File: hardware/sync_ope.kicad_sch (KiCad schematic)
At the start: 56 parts

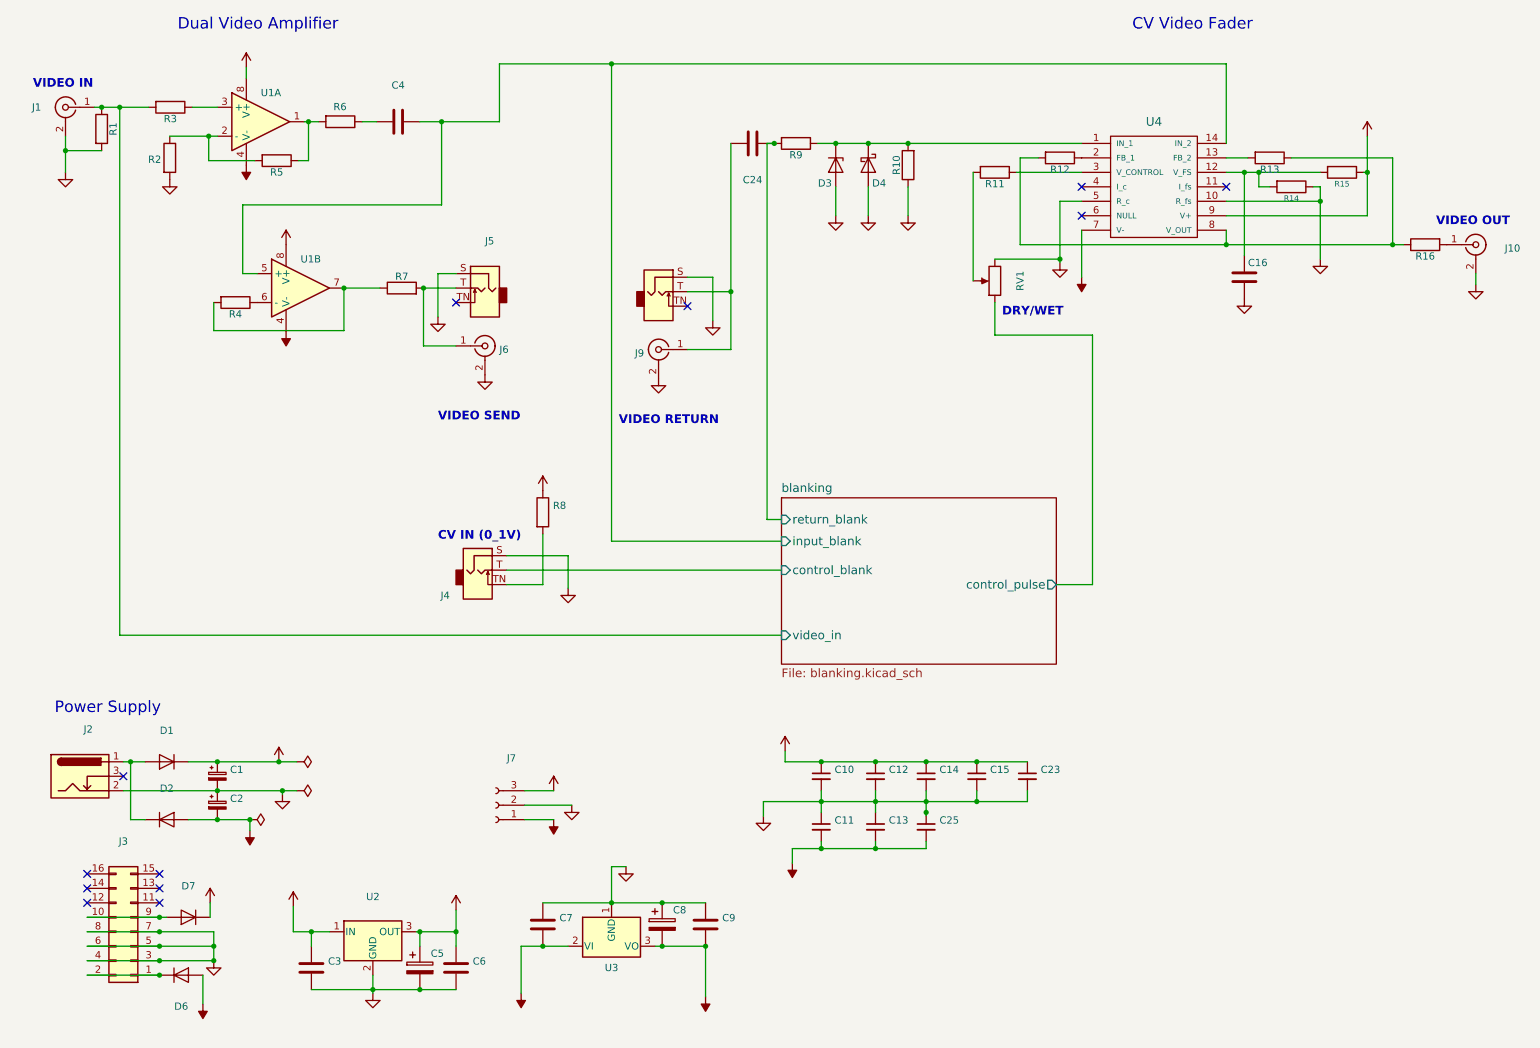
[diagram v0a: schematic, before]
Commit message: update blanking values
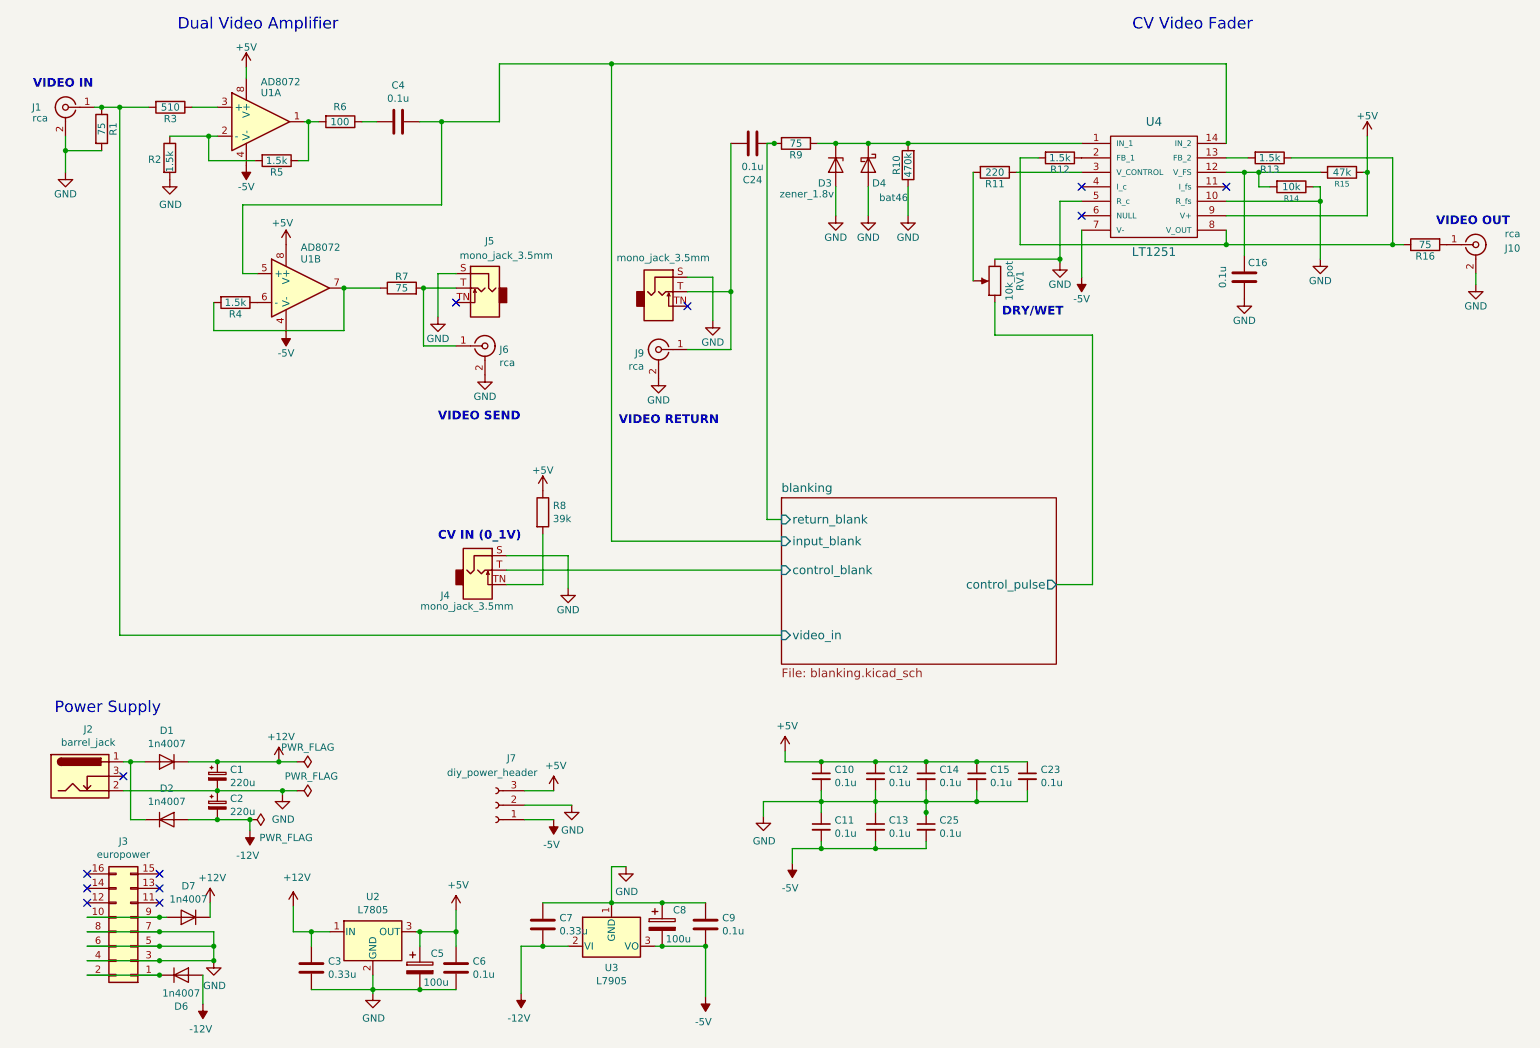
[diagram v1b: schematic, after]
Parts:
- C1, C2: value (none) -> 220u; footprint (none) -> Capacitor_THT:CP_Radial_D7.5mm_P2.50mm
- C10, C11, C12, C13, C14, C15, C16, C23, C24, C25, C4, C6, C9: value (none) -> 0.1u; footprint (none) -> Capacitor_THT:C_Disc_D4.3mm_W1.9mm_P5.00mm
- C3, C7: value (none) -> 0.33u; footprint (none) -> Capacitor_THT:C_Disc_D4.3mm_W1.9mm_P5.00mm
- C5, C8: value (none) -> 100u; footprint (none) -> Capacitor_THT:CP_Radial_D7.5mm_P2.50mm
- D1, D2, D6, D7: value (none) -> 1n4007; footprint (none) -> Diode_THT:D_DO-35_SOD27_P10.16mm_Horizontal
- D3: value (none) -> zener_1.8v; footprint (none) -> Diode_THT:D_DO-35_SOD27_P7.62mm_Horizontal
- D4: value (none) -> bat46; footprint (none) -> Diode_THT:D_DO-35_SOD27_P7.62mm_Horizontal
- J1, J10, J6, J9: value (none) -> rca; footprint (none) -> lib_fp:tht_vertical_rca
- J2: value (none) -> barrel_jack; footprint (none) -> Connector_BarrelJack:BarrelJack_Horizontal
- J3: value (none) -> europower; footprint (none) -> Connector_PinHeader_2.54mm:PinHeader_2x08_P2.54mm_Vertical
- J4, J5: value (none) -> mono_jack_3.5mm; footprint (none) -> lib_fp:Jack_3.5mm_QingPu_WQP-PJ398SM_Vertical_CircularHoles
- J7: value (none) -> diy_power_header; footprint (none) -> Connector_PinHeader_2.54mm:PinHeader_1x03_P2.54mm_Vertical
- J8: value (none) -> mono_jack_3.5mm; footprint (none) -> Connector_Audio:Jack_3.5mm_QingPu_WQP-PJ398SM_Vertical_CircularHoles
- R1, R16, R7, R9: value (none) -> 75; footprint (none) -> Resistor_THT:R_Axial_DIN0204_L3.6mm_D1.6mm_P7.62mm_Horizontal
- R10: value (none) -> 470k; footprint (none) -> Resistor_THT:R_Axial_DIN0204_L3.6mm_D1.6mm_P7.62mm_Horizontal
- R11: value (none) -> 220; footprint (none) -> Resistor_THT:R_Axial_DIN0204_L3.6mm_D1.6mm_P7.62mm_Horizontal
- R12, R13, R2, R4, R5: value (none) -> 1.5k; footprint (none) -> Resistor_THT:R_Axial_DIN0204_L3.6mm_D1.6mm_P7.62mm_Horizontal
- R14: value (none) -> 10k; footprint (none) -> Resistor_THT:R_Axial_DIN0204_L3.6mm_D1.6mm_P7.62mm_Horizontal
- R15: value (none) -> 47k; footprint (none) -> Resistor_THT:R_Axial_DIN0204_L3.6mm_D1.6mm_P7.62mm_Horizontal
- R3: value (none) -> 510; footprint (none) -> Resistor_THT:R_Axial_DIN0204_L3.6mm_D1.6mm_P7.62mm_Horizontal
- R6: value (none) -> 100; footprint (none) -> Resistor_THT:R_Axial_DIN0204_L3.6mm_D1.6mm_P7.62mm_Horizontal
- R8: value (none) -> 39k; footprint (none) -> Resistor_THT:R_Axial_DIN0204_L3.6mm_D1.6mm_P7.62mm_Horizontal
- RV1: value (none) -> 10k_pot; footprint (none) -> lib_fp:Potentiometer_Vertical_Large
- U1: value (none) -> AD8072; footprint (none) -> lib_fp:DIP-SOIC-8
- U2: value (none) -> L7805; footprint (none) -> Package_TO_SOT_THT:TO-220-3_Vertical
- U3: value (none) -> L7905; footprint (none) -> Package_TO_SOT_THT:TO-220-3_Vertical
- U4: value (none) -> LT1251; footprint (none) -> lib_fp:DIP+SOIC_14

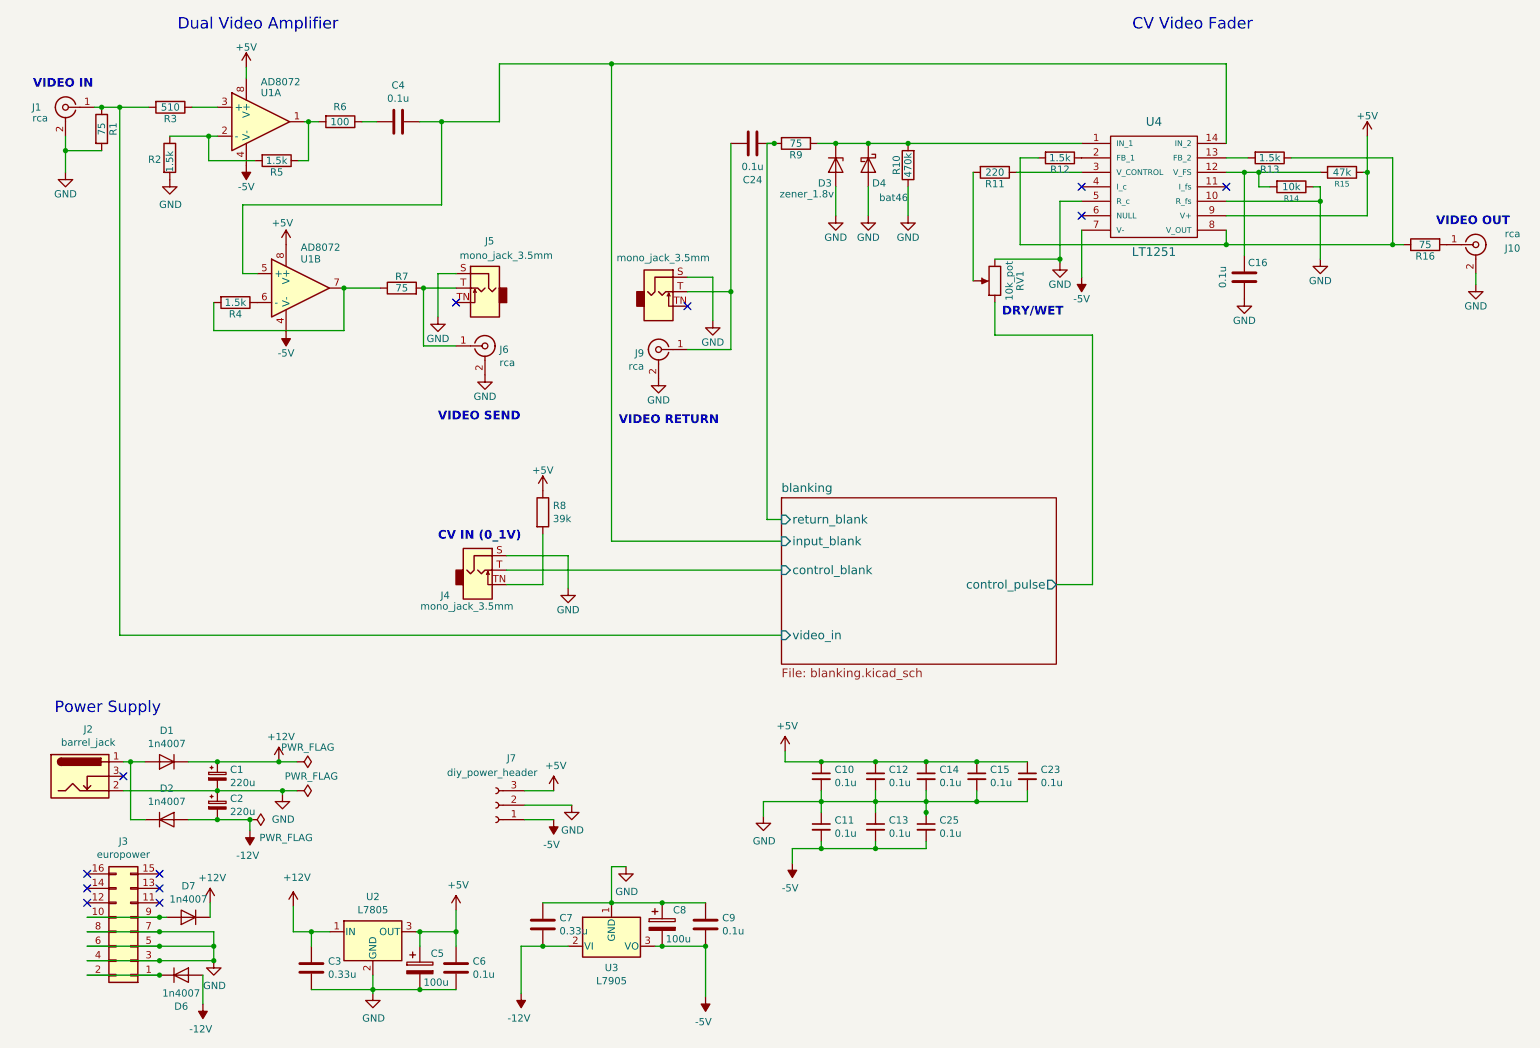
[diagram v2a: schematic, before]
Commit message: create revision for new power circuit
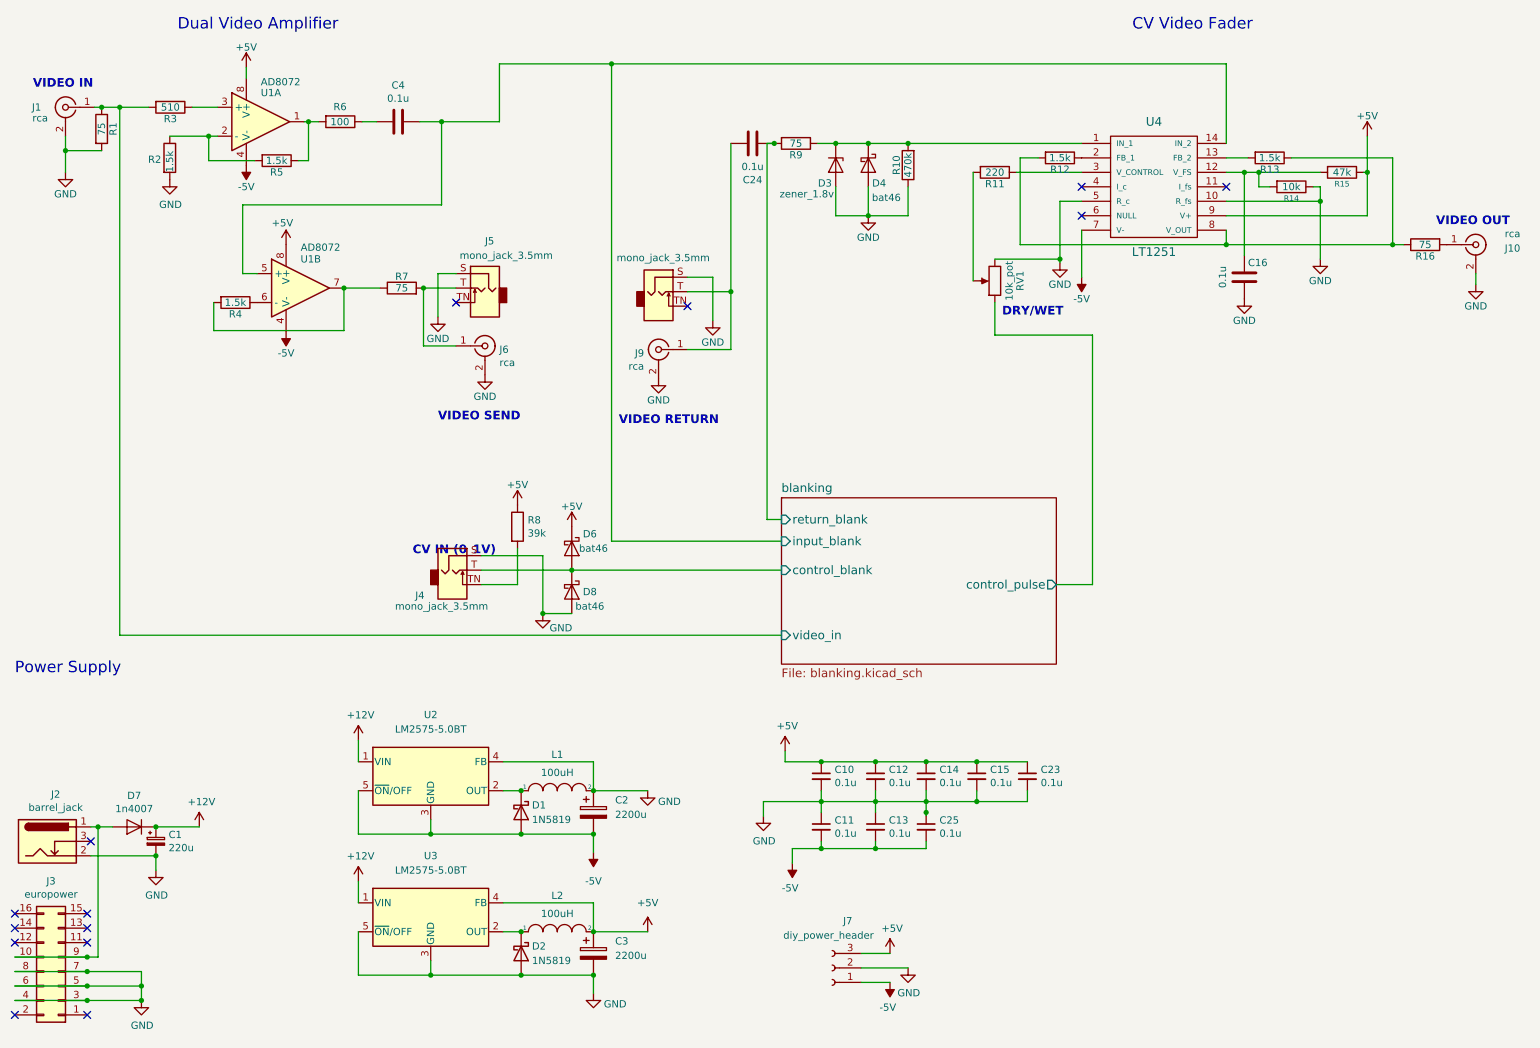
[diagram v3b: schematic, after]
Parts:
- removed C2: 220u, Capacitor_THT:CP_Radial_D7.5mm_P2.50mm, symbol Sync-Ope-proto-rescue:CP_Small-Device
- removed C3, C7: 0.33u, Capacitor_THT:C_Disc_D4.3mm_W1.9mm_P5.00mm, symbol Sync-Ope-proto-rescue:C-Device
- removed C5, C8: 100u, Capacitor_THT:CP_Radial_D7.5mm_P2.50mm, symbol Sync-Ope-proto-rescue:CP-Device
- removed C6, C9: 0.1u, Capacitor_THT:C_Disc_D4.3mm_W1.9mm_P5.00mm, symbol Sync-Ope-proto-rescue:C-Device
- removed D1, D2, D6: 1n4007, Diode_THT:D_DO-35_SOD27_P10.16mm_Horizontal, symbol Sync-Ope-proto-rescue:D-Device
- removed U2: L7805, Package_TO_SOT_THT:TO-220-3_Vertical, symbol Sync-Ope-proto-rescue:L7805-Regulator_Linear
- removed U3: L7905, Package_TO_SOT_THT:TO-220-3_Vertical, symbol Sync-Ope-proto-rescue:L7905-Regulator_Linear
- added C2, C3: 2200u, Capacitor_THT:CP_Radial_D13.0mm_P5.00mm, symbol Device:C_Polarized
- added D1, D2: 1N5819, Diode_THT:D_DO-41_SOD81_P7.62mm_Horizontal, symbol Device:D_Schottky
- added D6, D8: bat46, Diode_THT:D_DO-35_SOD27_P7.62mm_Horizontal, symbol Sync-Ope-proto-rescue:D_Schottky-Device
- added L1, L2: 100uH, Inductor_THT:L_Radial_D10.0mm_P5.00mm_Neosid_SD12k_style3, symbol pspice:INDUCTOR
- added U2, U3: LM2575-5.0BT, Package_TO_SOT_THT:TO-220-5_Vertical, symbol Regulator_Switching:LM2575-5.0BT
- C1: footprint Capacitor_THT:CP_Radial_D7.5mm_P2.50mm -> Capacitor_THT:CP_Radial_D5.0mm_P2.50mm
- J2: footprint Connector_BarrelJack:BarrelJack_Horizontal -> lib_fp:BarrelJack_Horizontal
- J8: footprint Connector_Audio:Jack_3.5mm_QingPu_WQP-PJ398SM_Vertical_CircularHoles -> lib_fp:Jack_3.5mm_QingPu_WQP-PJ398SM_Vertical_CircularHoles
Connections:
- net +12V: now also U2.1 (VIN), U3.1 (VIN)
- net +5V: now also C3.1, D6.1 (K), L2.2, U3.4 (FB)
- net -5V: now also C2.2, D1.2 (A), U2.3 (GND), U2.5 (~{ON}/OFF)
- net GND: now also C2.1, C3.2, D2.2 (A), D8.2 (A), L1.2, U2.4 (FB), U3.3 (GND), U3.5 (~{ON}/OFF)
- net blanking/control_blank: now also D6.2 (A), D8.1 (K)
- net at J3.1 (Pin_1): no longer J3.2 (Pin_2)
- net at D7.2 (A), J3.10 (Pin_10), J3.9 (Pin_9): now also J2.1
- new net: D2.1 (K), L2.1, U3.2 (OUT)
- new net: D1.1 (K), L1.1, U2.2 (OUT)
- no-connect marks 12 -> 14
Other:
- moved on the sheet: C1, D7, J2, J3, J4, J7, R8

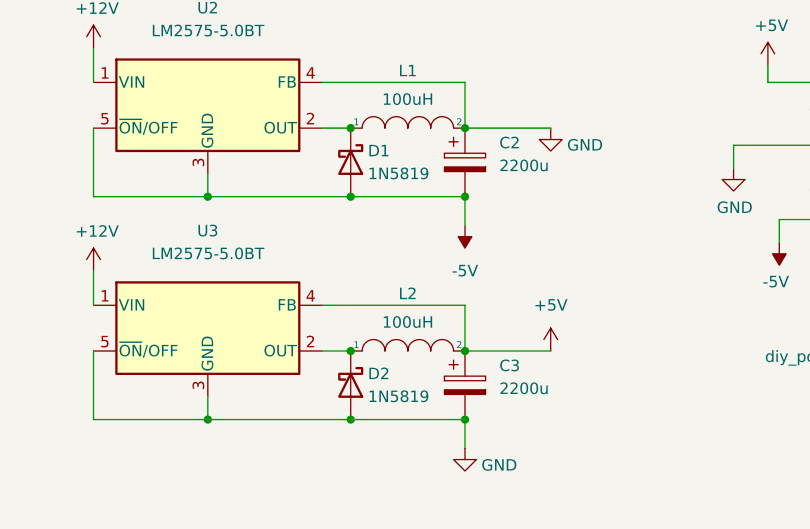
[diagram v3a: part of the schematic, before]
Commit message: update to v1_0_1 to increase range of blanking trim
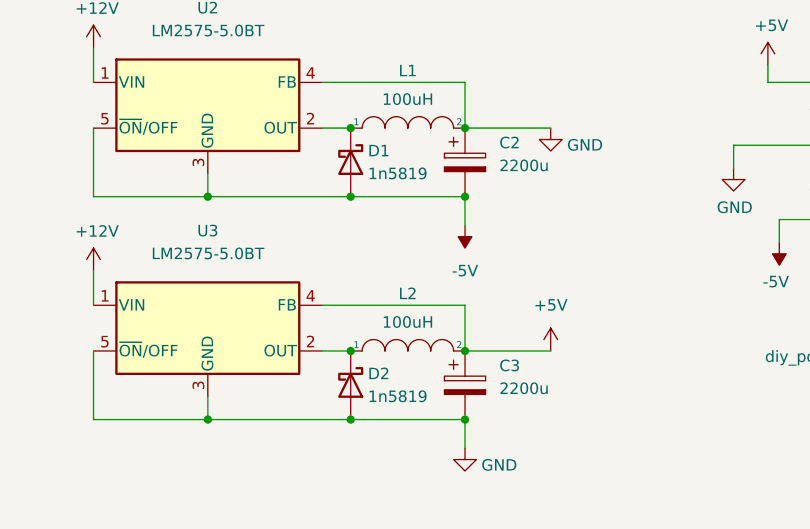
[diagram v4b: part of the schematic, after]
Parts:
- D1, D2: value 1N5819 -> 1n5819
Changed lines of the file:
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@@
     (title "sync_ope")
     (date "2022-11-24")
-    (rev "1.0.0")
+    (rev "1.0.1")
     (company "based on circuit design -byGaël Jaton")
     (comment 1 "updated by cyberboy666")
@@
       (effects (font (size 1.27 1.27)) (justify left))
     )
-    (property "Value" "1N5819" (id 1) (at 104.775 185.42 90)
+    (property "Value" "1n5819" (id 1) (at 104.775 185.42 90)
       (effects (font (size 1.27 1.27)) (justify left))
     )
@@
       (effects (font (size 1.27 1.27)) (justify left))
     )
-    (property "Value" "1N5819" (id 1) (at 104.775 160.655 90)
+    (property "Value" "1n5819" (id 1) (at 104.775 160.655 90)
       (effects (font (size 1.27 1.27)) (justify left))
     )
@@
     )
     (path "/bf960921-d501-4d3d-a988-849edc839478"
-      (reference "D1") (unit 1) (value "1N5819") (footprint "Diode_THT:D_DO-41_SOD81_P7.62mm_Horizontal")
+      (reference "D1") (unit 1) (value "1n5819") (footprint "Diode_THT:D_DO-41_SOD81_P7.62mm_Horizontal")
     )
     (path "/415bca51-8b22-4605-acfd-a559d5f85385"
-      (reference "D2") (unit 1) (value "1N5819") (footprint "Diode_THT:D_DO-41_SOD81_P7.62mm_Horizontal")
+      (reference "D2") (unit 1) (value "1n5819") (footprint "Diode_THT:D_DO-41_SOD81_P7.62mm_Horizontal")
     )
     (path "/00000000-0000-0000-0000-00005e4691b4"
@@
     )
     (path "/00000000-0000-0000-0000-00005fdd6789/00000000-0000-0000-0000-00006151f971"
-      (reference "R22") (unit 1) (value "22k") (footprint "Resistor_THT:R_Axial_DIN0204_L3.6mm_D1.6mm_P7.62mm_Horizontal")
+      (reference "R22") (unit 1) (value "12k") (footprint "Resistor_THT:R_Axial_DIN0204_L3.6mm_D1.6mm_P7.62mm_Horizontal")
     )
     (path "/00000000-0000-0000-0000-00005db76f3b"
@@
     )
     (path "/00000000-0000-0000-0000-00005fdd6789/00000000-0000-0000-0000-00006151f97c"
-      (reference "RV5") (unit 1) (value "10k_trim") (footprint "lib_fp:tht_vertical_trim_3362")
+      (reference "RV5") (unit 1) (value "20k_trim") (footprint "lib_fp:tht_vertical_trim_3362")
     )
     (path "/00000000-0000-0000-0000-00005db6bab3"
